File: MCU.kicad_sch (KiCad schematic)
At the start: 14 parts, among them J2 USB-C, J5 DIGITAL IO INPUTS, U3 ESP32-S3

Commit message: 9/18/2026 schematic work
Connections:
- net Vbus: now reaches D1.2 (VSS), J2.A4 (VBUS), J2.A9 (VBUS), J2.B4 (VBUS), J2.B9 (VBUS)
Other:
- note removed: "For Grayson: Connect Vbus to the input of the 3.3 V regulator (and the +5V net?) I think that will allow the entire device to work with only USB power. Use schottky diodes."
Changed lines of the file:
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@@
 		)
 	)
-	(text "For Grayson: Connect Vbus to the input of the 3.3 V regulator (and the +5V net?)\nI think that will allow the entire device to work with only USB power.\nUse schottky diodes."
-		(exclude_from_sim no)
-		(at 209.804 73.406 0)
-		(effects
-			(font
-				(size 1.27 1.27)
-			)
-		)
-	)
 	(junction
 		(at 175.26 91.44)
@@
 		)
 	)
+	(global_label "Vbus"
+		(shape input)
+		(at 172.72 83.82 180)
+		(fields_autoplaced yes)
+		(effects
+			(font
+				(size 1.27 1.27)
+			)
+			(justify right)
+		)
+		(property "Intersheetrefs" "${INTERSHEET_REFS}"
+			(at 165.3201 83.82 0)
+			(hide yes)
+			(show_name no)
+			(do_not_autoplace no)
+			(effects
+				(font
+					(size 1.27 1.27)
+				)
+				(justify right)
+			)
+		)
+	)
 	(global_label "CS0_ADC"
 		(shape input)
@@
 			)
 		)
+		(property "Mouser Link" ""
+			(at 121.92 157.48 0)
+			(hide yes)
+			(show_name no)
+			(do_not_autoplace no)
+			(effects
+				(font
+					(size 1.27 1.27)
+				)
+			)
+		)
 		(pin "2"
 		)
@@
 			)
 		)
+		(property "Mouser Link" ""
+			(at 81.28 106.68 0)
+			(hide yes)
+			(show_name no)
+			(do_not_autoplace no)
+			(effects
+				(font
+					(size 1.27 1.27)
+				)
+			)
+		)
 		(pin "1"
 		)
@@
 			)
 		)
+		(property "Mouser Link" ""
+			(at 191.77 111.76 0)
+			(hide yes)
+			(show_name no)
+			(do_not_autoplace no)
+			(effects
+				(font
+					(size 1.27 1.27)
+				)
+			)
+		)
 		(pin "2"
 		)
@@
 			)
 		)
+		(property "Mouser Link" ""
+			(at 124.46 55.88 0)
+			(hide yes)
+			(show_name no)
+			(do_not_autoplace no)
+			(effects
+				(font
+					(size 1.27 1.27)
+				)
+			)
+		)
 		(pin "1"
 		)
@@
 			)
 		)
+		(property "Mouser Link" ""
+			(at 104.14 168.91 90)
+			(hide yes)
+			(show_name no)
+			(do_not_autoplace no)
+			(effects
+				(font
+					(size 1.27 1.27)
+				)
+			)
+		)
 		(pin "2"
 		)
@@
 			)
 		)
+		(property "Mouser Link" ""
+			(at 104.14 157.48 0)
+			(hide yes)
+			(show_name no)
+			(do_not_autoplace no)
+			(effects
+				(font
+					(size 1.27 1.27)
+				)
+			)
+		)
 		(pin "2"
 		)
@@
 			)
 		)
+		(property "Mouser Link" ""
+			(at 99.06 69.85 0)
+			(hide yes)
+			(show_name no)
+			(do_not_autoplace no)
+			(effects
+				(font
+					(size 1.27 1.27)
+				)
+			)
+		)
 		(pin "2"
 		)
@@
 			)
 		)
+		(property "Mouser Link" ""
+			(at 208.28 88.9 90)
+			(hide yes)
+			(show_name no)
+			(do_not_autoplace no)
+			(effects
+				(font
+					(size 1.27 1.27)
+				)
+			)
+		)
 		(pin "1"
 		)
@@
 			)
 		)
+		(property "Mouser Link" ""
+			(at 121.92 168.91 90)
+			(hide yes)
+			(show_name no)
+			(do_not_autoplace no)
+			(effects
+				(font
+					(size 1.27 1.27)
+				)
+			)
+		)
 		(pin "2"
 		)
@@
 			)
 		)
+		(property "Mouser Link" ""
+			(at 106.68 74.93 0)
+			(hide yes)
+			(show_name no)
+			(do_not_autoplace no)
+			(effects
+				(font
+					(size 1.27 1.27)
+				)
+			)
+		)
 		(pin "1"
 		)
@@
 			)
 		)
+		(property "Mouser Link" ""
+			(at 135.89 104.14 0)
+			(hide yes)
+			(show_name no)
+			(do_not_autoplace no)
+			(effects
+				(font
+					(size 1.27 1.27)
+				)
+			)
+		)
 		(pin "5"
 		)
@@
 			)
 		)
+		(property "Mouser Link" ""
+			(at 113.03 55.88 0)
+			(hide yes)
+			(show_name no)
+			(do_not_autoplace no)
+			(effects
+				(font
+					(size 1.27 1.27)
+				)
+			)
+		)
 		(pin "1"
 		)
@@
 			)
 		)
+		(property "Mouser Link" ""
+			(at 208.28 91.44 90)
+			(hide yes)
+			(show_name no)
+			(do_not_autoplace no)
+			(effects
+				(font
+					(size 1.27 1.27)
+				)
+			)
+		)
 		(pin "2"
 		)
@@
 			(at 233.68 99.06 0)
 			(hide yes)
+			(show_name no)
+			(do_not_autoplace no)
+			(effects
+				(font
+					(size 1.27 1.27)
+				)
+			)
+		)
+		(property "Mouser Link" ""
+			(at 233.68 99.06 0)
+			(hide yes)

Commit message: removed grounds from inputs
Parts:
- removed J5: DIGITAL IO INPUTS, symbol Connector_Generic:Conn_01x09
- added J2: DIGITAL IO INPUTS, symbol Connector_Generic:Conn_01x08
- renumbered C5 to C7, C20 to C8, C4 to C9, D2 to D3, D3 to D4, D1 to D5, J2 to J3, R34 to R3, R3 to R4, R4 to R5
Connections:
- net DIO1: now also J2.1 (Pin_1)
- net DIO2: now also J2.2 (Pin_2)
- net DIO3: now also J2.3 (Pin_3)
- net DIO4: now also J2.4 (Pin_4)
- net DIO5: now also J2.5 (Pin_5)
- net DIO6: now also J2.6 (Pin_6)
- net DIO7: now also J2.7 (Pin_7)
- net DIO8: now also J2.8 (Pin_8)

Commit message: 9/20/2026 schematic work
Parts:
- C7: footprint (none) -> Capacitor_SMD:C_1206_3216Metric_Pad1.33x1.80mm_HandSolder; MPN (none) -> GRM31CR71E105KA01L; Mouser Link (none) -> https://www.mouser.com/en/ProductDetail/Murata-Electronics/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
- C8: footprint (none) -> Capacitor_SMD:C_1206_3216Metric_Pad1.33x1.80mm_HandSolder; MPN (none) -> GRM31CR71A226KE15L; Mouser Link (none) -> https://www.mouser.com/en/ProductDetail/Murata-Electronics/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
- C9: footprint (none) -> Capacitor_SMD:C_1206_3216Metric_Pad1.33x1.80mm_HandSolder; MPN (none) -> GRM31CR72E104KW03L; Mouser Link (none) -> https://www.mouser.com/en/ProductDetail/Murata-Electronics/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
- D5: renamed from D3; value TLHR-6400 -> POWER_LED; footprint LED_THT:LED_D5.0mm -> LED_THT:LED_D5.0mm_Horizontal_O1.27mm_Z3.0mm; MPN TLHR6400 -> WP7113ID; Mouser Link (none) -> https://www.mouser.com/en/ProductDetail/Kingbright/WP7113ID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
- D6: renamed from D4; value TLHY-6400 -> WIFI_LED; footprint LED_THT:LED_D5.0mm -> LED_THT:LED_D5.0mm_Horizontal_O1.27mm_Z3.0mm; MPN TLHY6400 -> WP7113YD; Mouser Link (none) -> https://www.mouser.com/en/ProductDetail/Kingbright/WP7113YD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
- J3: footprint Connector_USB:USB_C_Plug_JAE_DX07P024AJ1 -> Connector_USB:USB_C_Receptacle_GCT_USB4110; Mouser Link (none) -> https://www.mouser.com/en/ProductDetail/GCT/USB4110-GF-A?qs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
- R3: renamed from R1; footprint (none) -> Resistor_SMD:R_1206_3216Metric_Pad1.30x1.75mm_HandSolder; MPN (none) -> RC1206DR-0710KL; Mouser Link (none) -> https://www.mouser.com/en/ProductDetail/YAGEO/RC1206DR-0710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
- R4: renamed from R2; value 330R -> 100R; footprint (none) -> Resistor_SMD:R_1206_3216Metric_Pad1.30x1.75mm_HandSolder; MPN (none) -> RC1206DR-07100RL; Mouser Link (none) -> https://www.mouser.com/en/ProductDetail/YAGEO/RC1206DR-0710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
- R5: renamed from R3; value 330R -> 100R; footprint (none) -> Resistor_SMD:R_1206_3216Metric_Pad1.30x1.75mm_HandSolder; MPN (none) -> RC1206DR-07100RL; Mouser Link (none) -> https://www.mouser.com/en/ProductDetail/YAGEO/RC1206DR-0710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
- R6: renamed from R4; footprint (none) -> Resistor_SMD:R_1206_3216Metric_Pad1.30x1.75mm_HandSolder; MPN (none) -> AC1206FR-075K1L; Mouser Link (none) -> https://www.mouser.com/en/ProductDetail/YAGEO/AC1206FR-075K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
- R7: renamed from R5; footprint (none) -> Resistor_SMD:R_1206_3216Metric_Pad1.30x1.75mm_HandSolder; MPN (none) -> AC1206FR-075K1L; Mouser Link (none) -> https://www.mouser.com/en/ProductDetail/YAGEO/AC1206FR-075K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
- U3: MPN ESP32-S3-WROOM-1-N16R8 -> ESP32-S3-WROOM-1-N8R2; Mouser Link (none) -> https://www.mouser.com/en/ProductDetail/Espressif-Systems/E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
- U4: renamed from D5; MPN DT1042-04SO-7 -> DT1042-04SOQ-7; Mouser Link (none) -> https://www.mouser.com/en/ProductDetail/Diodes-Incorporated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
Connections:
- net GND: now also U4.2 (VSS); no longer U4.5 (VCC)
- net Vbus: now also U4.5 (VCC); no longer U4.2 (VSS)
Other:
- note added: "Place as close to USB connector as possible."
- note removed: "Add TVS arrays if needed"
- company: Slap DAQ -> Faster Than Sound
- title: MCU -> SlapDAQ - MCU
- moved on the sheet: U4

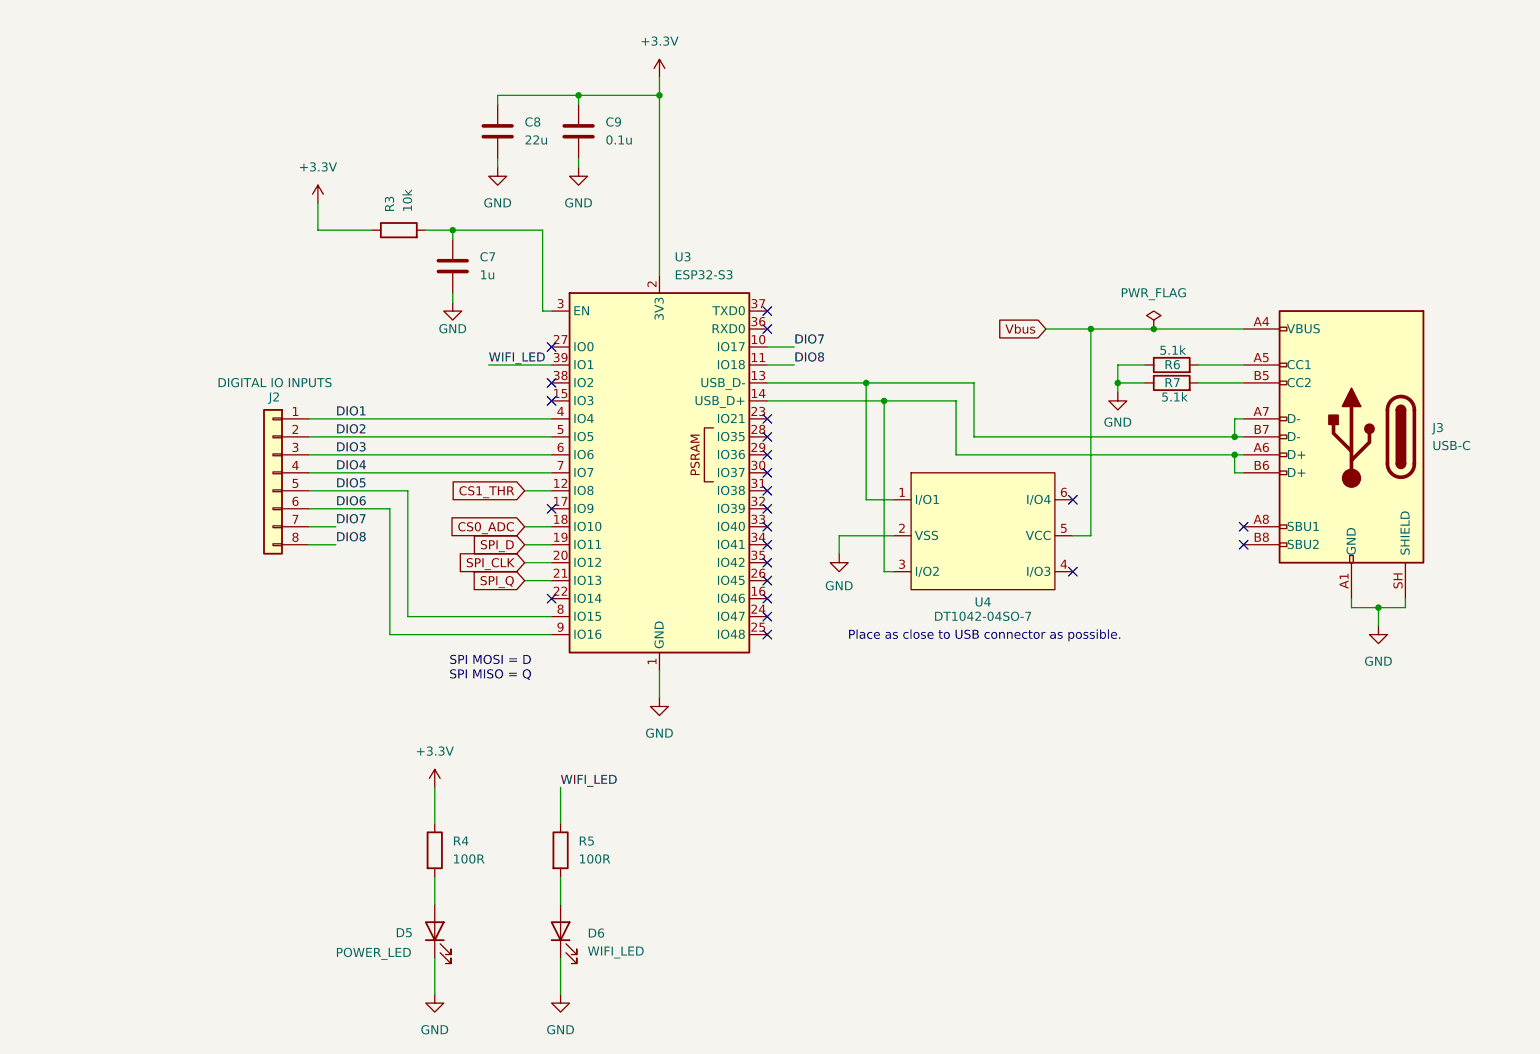
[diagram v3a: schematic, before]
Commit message: Add screw terminals
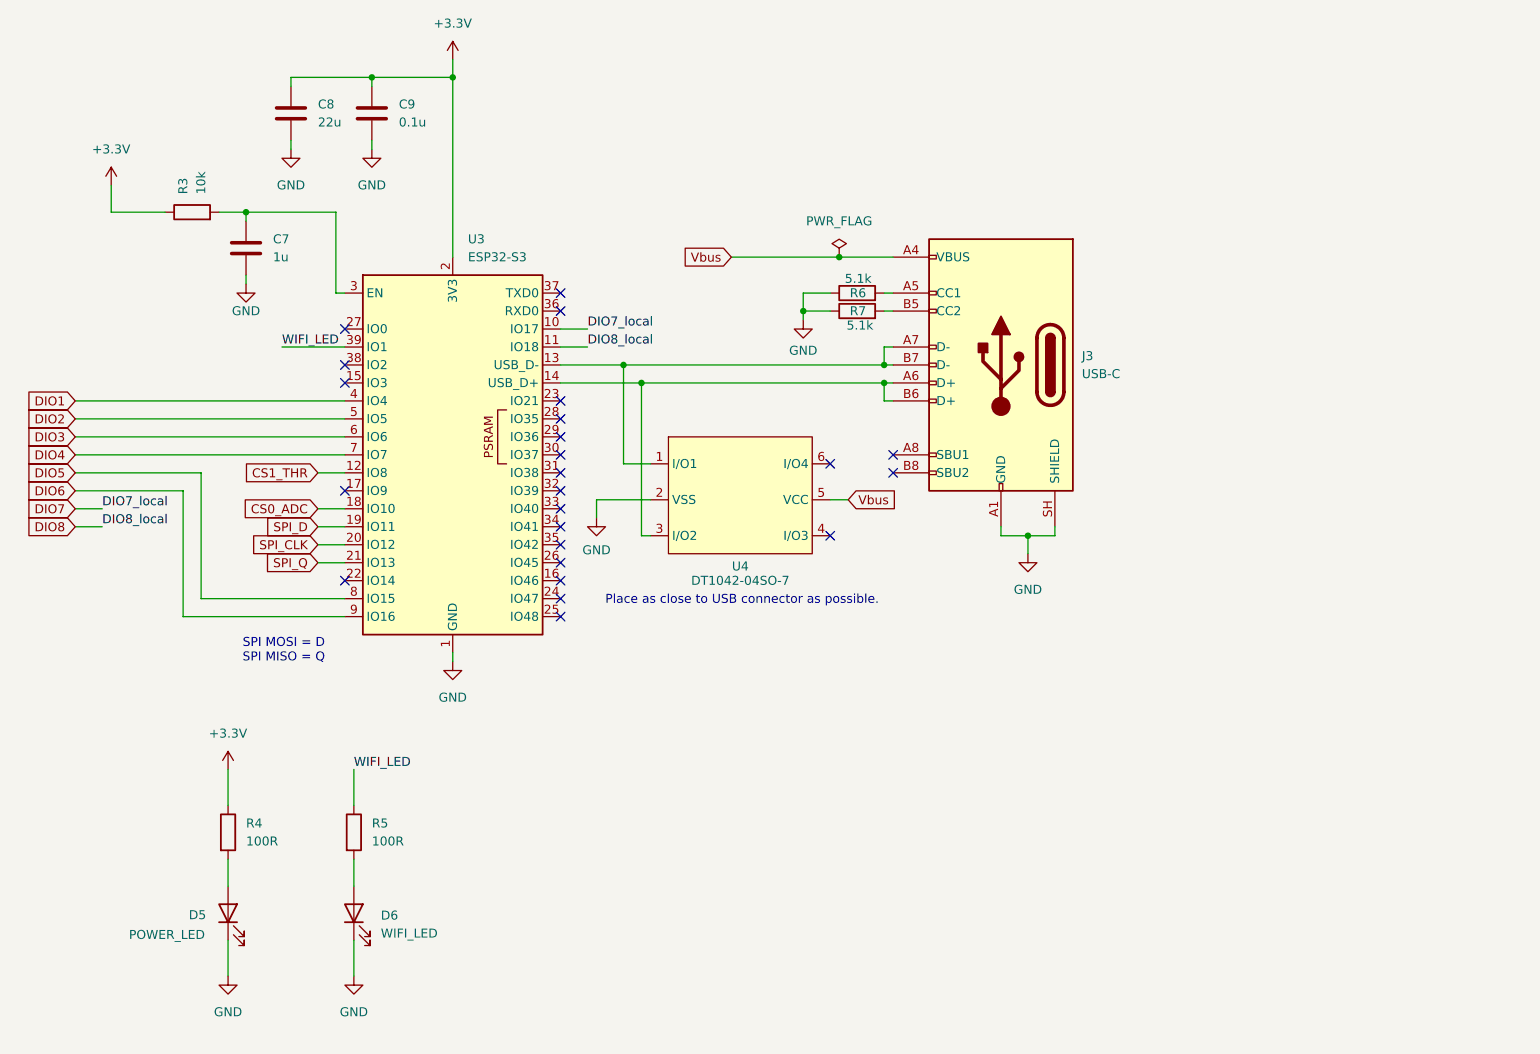
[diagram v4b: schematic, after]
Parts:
- removed J2: DIGITAL IO INPUTS, symbol Connector_Generic:Conn_01x08
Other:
- moved on the sheet: C7, C8, C9, D5, D6, J3, R3, R4, R5, R6, R7, U3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

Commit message: Add 3D models and rearrange pins
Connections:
- net DIO8 is gone; now on net DIO7: U3.11 (IO18)
- net DIO1: now also U3.5 (IO5); no longer U3.4 (IO4)
- net DIO2: now also U3.6 (IO6); no longer U3.5 (IO5)
- net DIO3: now also U3.7 (IO7); no longer U3.6 (IO6)
- net DIO4: now also U3.8 (IO15); no longer U3.7 (IO7)
- net DIO5: now also U3.9 (IO16); no longer U3.8 (IO15)
- net DIO6: now also U3.10 (IO17); no longer U3.9 (IO16)
- net DIO7: no longer U3.10 (IO17)
- new net DIO0: U3.4 (IO4)

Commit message: Finish rev. 1 PCB
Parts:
- C8: MPN GRM31CR71A226KE15L -> GCM31CR71A226KE02L; Mouser Link https://www.mouser.com/en/ProductDetail/Murata-Electronics/GRM31CR71A226KE15L?qs=%2FBLjsTEvPnhfnPGA5Hlk4g%3D%3D -> https://www.mouser.com/en/ProductDetail/Murata-Electronics/GCM31CR71A226KE02L?qs=9UHcxq0qN4vtutbd1jidnA%3D%3D
- U3: MPN ESP32-S3-WROOM-1-N8R2 -> ESP32-S3-WROOM-1-N16R8; Mouser Link https://www.mouser.com/en/ProductDetail/Espressif-Systems/ESP32-S3-WROOM-1-N8R2?qs=Wj%2FVkw3K%252BMCC1Ha9x85iJA%3D%3D -> https://www.mouser.com/en/ProductDetail/Espressif-Systems/ESP32-S3-WROOM-1-N16R8?qs=Li%252BoUPsLEnvQc9gW6AMhZg%3D%3D
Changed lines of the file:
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@@
 			)
 		)
-		(property "MPN" "ESP32-S3-WROOM-1-N8R2"
+		(property "MPN" "ESP32-S3-WROOM-1-N16R8"
 			(at 106.68 101.6 0)
 			(hide yes)
@@
 			)
 		)
-		(property "Mouser Link" "https://www.mouser.com/en/ProductDetail/Espressif-Systems/ESP32-S3-WROOM-1-N8R2?qs=Wj%2FVkw3K%252BMCC1Ha9x85iJA%3D%3D"
+		(property "Mouser Link" "https://www.mouser.com/en/ProductDetail/Espressif-Systems/ESP32-S3-WROOM-1-N16R8?qs=Li%252BoUPsLEnvQc9gW6AMhZg%3D%3D"
 			(at 106.68 101.6 0)
 			(hide yes)
@@
 			)
 		)
-		(property "Mouser Link" "https://www.mouser.com/en/ProductDetail/Murata-Electronics/GRM31CR71A226KE15L?qs=%2FBLjsTEvPnhfnPGA5Hlk4g%3D%3D"
+		(property "Mouser Link" "https://www.mouser.com/en/ProductDetail/Murata-Electronics/GCM31CR71A226KE02L?qs=9UHcxq0qN4vtutbd1jidnA%3D%3D"
 			(at 83.82 53.34 0)
 			(hide yes)
@@
 			)
 		)
-		(property "MPN" "GRM31CR71A226KE15L"
+		(property "MPN" "GCM31CR71A226KE02L"
 			(at 83.82 53.34 0)
 			(hide yes)
